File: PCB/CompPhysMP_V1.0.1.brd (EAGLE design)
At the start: 157.5 x 50.8 mm, 28 parts, among them J1 STX-3000, J2 STX-3000, Q1 BSS123, Q2 BSS123, Q3 BSS123, Q4 BSS123, X1 DIPMICRO-BUZZER6P5_7P5

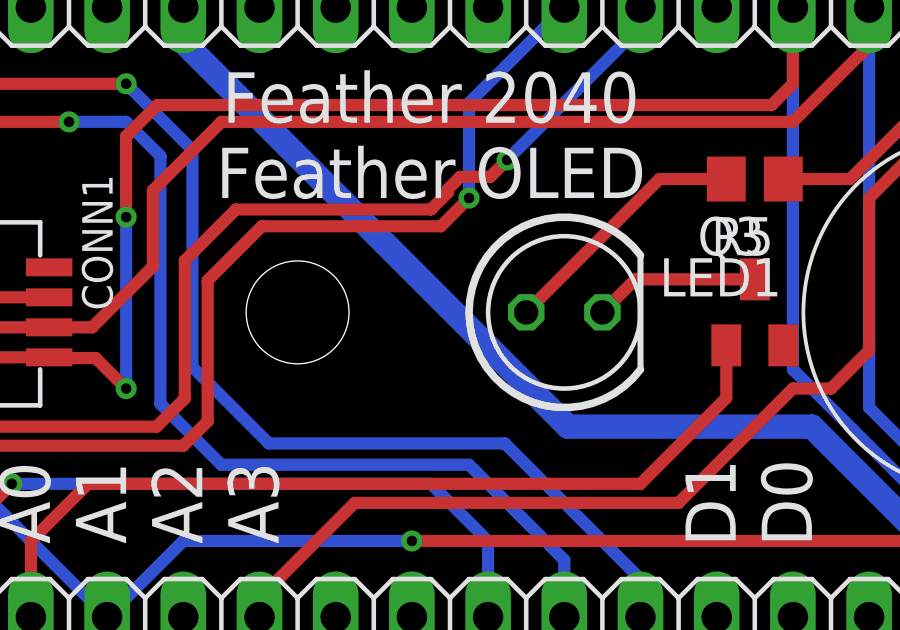
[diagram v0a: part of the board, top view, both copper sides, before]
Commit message: Updated PCB V1.0.1
Updated the resistance values from 1000 to 1K
Updated speaker resistor to 120
Updated LED resistor to 63
Updated fiducial names from FDn FDIn
Added .mnt file.
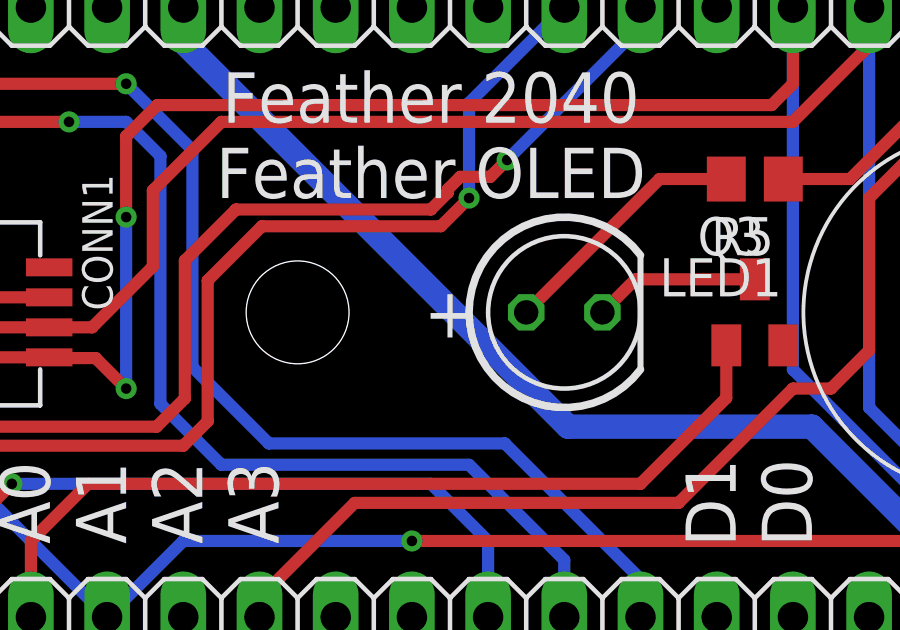
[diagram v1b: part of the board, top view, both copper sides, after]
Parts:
- R1, R2, R3, R4: value 1000 -> 1K
- R5: value 150 -> 63
- R6: value 150 -> 120
- renumbered FD1 to FID1, FD2 to FID2, FD3 to FID3
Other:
- board text added: "+"
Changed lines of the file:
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@@
 <text x="58.42" y="21.59" size="1.27" layer="22" font="vector" ratio="15" rot="MR90" align="bottom-center">-</text>
 <text x="58.42" y="19.05" size="1.27" layer="22" font="vector" ratio="15" rot="MR90" align="bottom-center">3V</text>
+<text x="5.08" y="0" size="1.6764" layer="21" font="vector" rot="SR0" align="center">+</text>
 </plain>
 <attributes>
@@
 </autorouter>
 <elements>
-<element name="FD1" library="Fiducial" package="FID_050" value="FID_50MIL" x="-22.225" y="-12.7" smashed="yes"/>
-<element name="FD2" library="Fiducial" package="FID_050" value="FID_50MIL" x="76.835" y="8.89" smashed="yes"/>
-<element name="FD3" library="Fiducial" package="FID_050" value="FID_50MIL" x="-22.225" y="10.16" smashed="yes"/>
+<element name="FID1" library="Fiducial" package="FID_050" value="FID_50MIL" x="-22.225" y="-12.7" smashed="yes"/>
+<element name="FID2" library="Fiducial" package="FID_050" value="FID_50MIL" x="76.835" y="8.89" smashed="yes"/>
+<element name="FID3" library="Fiducial" package="FID_050" value="FID_50MIL" x="-22.225" y="10.16" smashed="yes"/>
 <element name="JP4" library="pinhead" library_urn="urn:adsk.eagle:library:325" package="1X13" package3d_urn="urn:adsk.eagle:package:22421/2" value="" x="-59.69" y="-7.62" smashed="yes">
 <attribute name="NAME" x="-76.2762" y="-5.7912" size="1.27" layer="25" ratio="10"/>
@@
 <attribute name="VALUE" x="58.42" y="-2.54" size="1.27" layer="27"/>
 </element>
-<element name="R1" library="rcl" library_urn="urn:adsk.eagle:library:334" package="R0805" package3d_urn="urn:adsk.eagle:package:23553/2" value="1000" x="60.325" y="-3.175" smashed="yes">
+<element name="R1" library="rcl" library_urn="urn:adsk.eagle:library:334" package="R0805" package3d_urn="urn:adsk.eagle:package:23553/2" value="1K" x="60.325" y="-3.175" smashed="yes">
 <attribute name="NAME" x="59.69" y="-1.905" size="1.27" layer="25"/>
 <attribute name="POPULARITY" value="85" x="60.325" y="-3.175" size="1.778" layer="27" display="off"/>
@@
 <attribute name="VALUE" x="59.69" y="-5.715" size="1.27" layer="27"/>
 </element>
-<element name="R2" library="rcl" library_urn="urn:adsk.eagle:library:334" package="R0805" package3d_urn="urn:adsk.eagle:package:23553/2" value="1000" x="60.325" y="3.81" smashed="yes" rot="R180">
+<element name="R2" library="rcl" library_urn="urn:adsk.eagle:library:334" package="R0805" package3d_urn="urn:adsk.eagle:package:23553/2" value="1K" x="60.325" y="3.81" smashed="yes" rot="R180">
 <attribute name="NAME" x="60.96" y="2.54" size="1.27" layer="25" rot="R180"/>
 <attribute name="POPULARITY" value="85" x="60.325" y="3.81" size="1.778" layer="27" rot="R180" display="off"/>
@@
 <attribute name="VALUE" x="64.135" y="-2.54" size="1.27" layer="27"/>
 </element>
-<element name="R3" library="rcl" library_urn="urn:adsk.eagle:library:334" package="R0805" package3d_urn="urn:adsk.eagle:package:23553/2" value="1000" x="66.04" y="-3.175" smashed="yes">
+<element name="R3" library="rcl" library_urn="urn:adsk.eagle:library:334" package="R0805" package3d_urn="urn:adsk.eagle:package:23553/2" value="1K" x="66.04" y="-3.175" smashed="yes">
 <attribute name="NAME" x="65.405" y="-1.905" size="1.27" layer="25"/>
 <attribute name="POPULARITY" value="85" x="66.04" y="-3.175" size="1.778" layer="27" display="off"/>
@@
 <attribute name="VALUE" x="65.405" y="-5.715" size="1.27" layer="27"/>
 </element>
-<element name="R4" library="rcl" library_urn="urn:adsk.eagle:library:334" package="R0805" package3d_urn="urn:adsk.eagle:package:23553/2" value="1000" x="66.04" y="3.81" smashed="yes" rot="R180">
+<element name="R4" library="rcl" library_urn="urn:adsk.eagle:library:334" package="R0805" package3d_urn="urn:adsk.eagle:package:23553/2" value="1K" x="66.04" y="3.81" smashed="yes" rot="R180">
 <attribute name="NAME" x="66.675" y="2.54" size="1.27" layer="25" rot="R180"/>
 <attribute name="POPULARITY" value="85" x="70.485" y="8.255" size="1.778" layer="27" rot="R180" display="off"/>
@@
 <attribute name="VALUE" x="13.335" y="-3.175" size="1.27" layer="27"/>
 </element>
-<element name="R5" library="rcl" library_urn="urn:adsk.eagle:library:334" package="R0805" package3d_urn="urn:adsk.eagle:package:23553/2" value="150" x="15.24" y="4.445" smashed="yes" rot="R180">
+<element name="R5" library="rcl" library_urn="urn:adsk.eagle:library:334" package="R0805" package3d_urn="urn:adsk.eagle:package:23553/2" value="63" x="15.24" y="4.445" smashed="yes" rot="R180">
 <attribute name="NAME" x="15.875" y="3.175" size="1.27" layer="25" rot="R180"/>
 <attribute name="POPULARITY" value="85" x="15.24" y="4.445" size="1.778" layer="27" rot="R180" display="off"/>
@@
 <attribute name="VALUE" x="28.575" y="-6.985" size="1.27" layer="27"/>
 </element>
-<element name="R6" library="rcl" library_urn="urn:adsk.eagle:library:334" package="R0805" package3d_urn="urn:adsk.eagle:package:23553/2" value="150" x="30.48" y="5.715" smashed="yes" rot="R180">
+<element name="R6" library="rcl" library_urn="urn:adsk.eagle:library:334" package="R0805" package3d_urn="urn:adsk.eagle:package:23553/2" value="120" x="30.48" y="5.715" smashed="yes" rot="R180">
 <attribute name="NAME" x="31.115" y="4.445" size="1.27" layer="25" rot="R180"/>
 <attribute name="POPULARITY" value="85" x="30.48" y="4.445" size="1.778" layer="27" rot="R180" display="off"/>
